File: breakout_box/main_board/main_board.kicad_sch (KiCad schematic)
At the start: 35 parts, among them CN1 19PIN_LEMO, Q1 DMP3099L, Q2 MJD122

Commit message: Update schematics
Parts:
- C1, C2, C3, C4: footprint main_board:140CLH-1010 -> Capacitor_SMD:CP_Elec_10x10; symbol main_board-eagle-import:CPOL-EU140CLH-1010 -> Device:C_Polarized
- C5, C6: symbol main_board-eagle-import:C-EUC0603 -> Device:C
- H1, H2: symbol main_board-eagle-import:MA20-1 -> Connector_Generic:Conn_01x20
- H17, H3, H4, H7, H8: symbol main_board-eagle-import:MA08-1 -> Connector_Generic:Conn_01x08
- JP1, JP10, JP11, JP12, JP13, JP2, JP3, JP4, JP5, JP6, JP7, JP8, JP9: symbol main_board-eagle-import:PINHD-1X03_2.00 -> Connector_Generic:Conn_01x03
- R1, R2, R3: symbol main_board-eagle-import:R-EU_R0603 -> Device:R
- R4: symbol main_board-eagle-import:R-EU_R0402 -> Device:R
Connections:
- net GND: now also C1.2, C2.2, C3.2, C4.2; no longer C1.-, C2.-, C3.-, C4.-
- net V_AUX: now also C1.1; no longer C1.+
- net V_OUT: now also C4.1; no longer C4.+
- net at Q2.1 (B), R2.1, R3.2: now also C3.1; no longer C3.+
- net at R1.1, R2.2: now also C2.1; no longer C2.+
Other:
- note added: "19P LEMO Connector"
- note removed: "AGND"
- note removed: "CH1"
- note removed: "CH10"
- note removed: "CH10_A"
- note removed: "CH10_CV"
- note removed: "CH11"
- note removed: "CH11_A"
- note removed: "CH12"
- note removed: "CH12_A"
- note removed: "CH13"
- note removed: "CH13_A"
- note removed: "CH14"
- note removed: "CH14_A"
- note removed: "CH15"
- note removed: "CH15_A"
- note removed: "CH2"
- note removed: "CH3"
- note removed: "CH4"
- note removed: "CH5"
- note removed: "CH6"
- note removed: "CH7"
- note removed: "CH8"
- note removed: "CH9"
- note removed: "CH9_A"
- note removed: "DGND"
- note removed: "From 19P LEMO Connector"
- note removed: "V_AUX"
- note removed: "V_OUT"
- moved on the sheet: CN1, LED1, Q1, Q2

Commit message: Bump version to 2.6
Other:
- note removed: "v2.5"
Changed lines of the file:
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@@
   (title_block
     (title "Nexus Main Board")
-    (date "2022-08-29")
-    (rev "2.51")
+    (date "2023-03-05")
+    (rev "2.6")
     (company "Document Number: 2022011")
   )
@@
     (effects (font (size 2.54 2.159)) (justify right bottom))
   )
-  (text "v2.5" (at 408.94 276.86 180)
-    (effects (font (size 2.54 2.54)) (justify left bottom))
-  )
   (text "GND" (at 128.905 201.295 180)

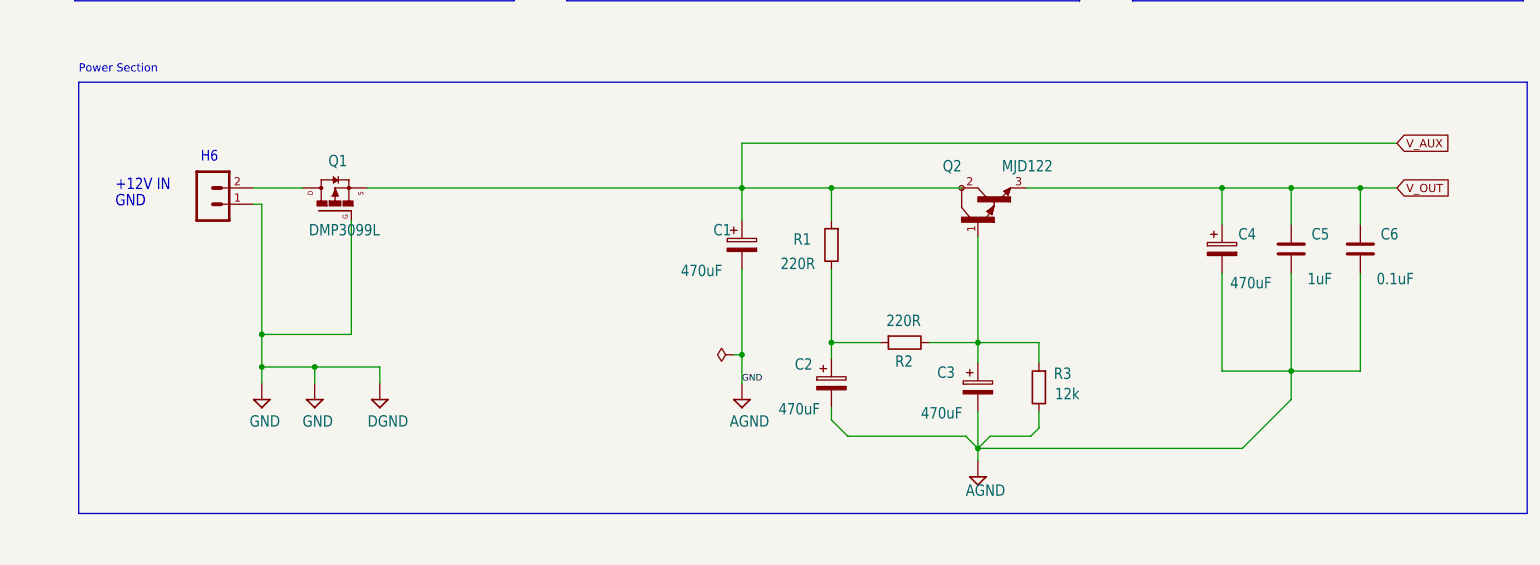
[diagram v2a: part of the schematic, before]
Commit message: Upgrade to v2.6 - Added short circuit protection - Added soft power switch - Various schematics and PCB layout updates
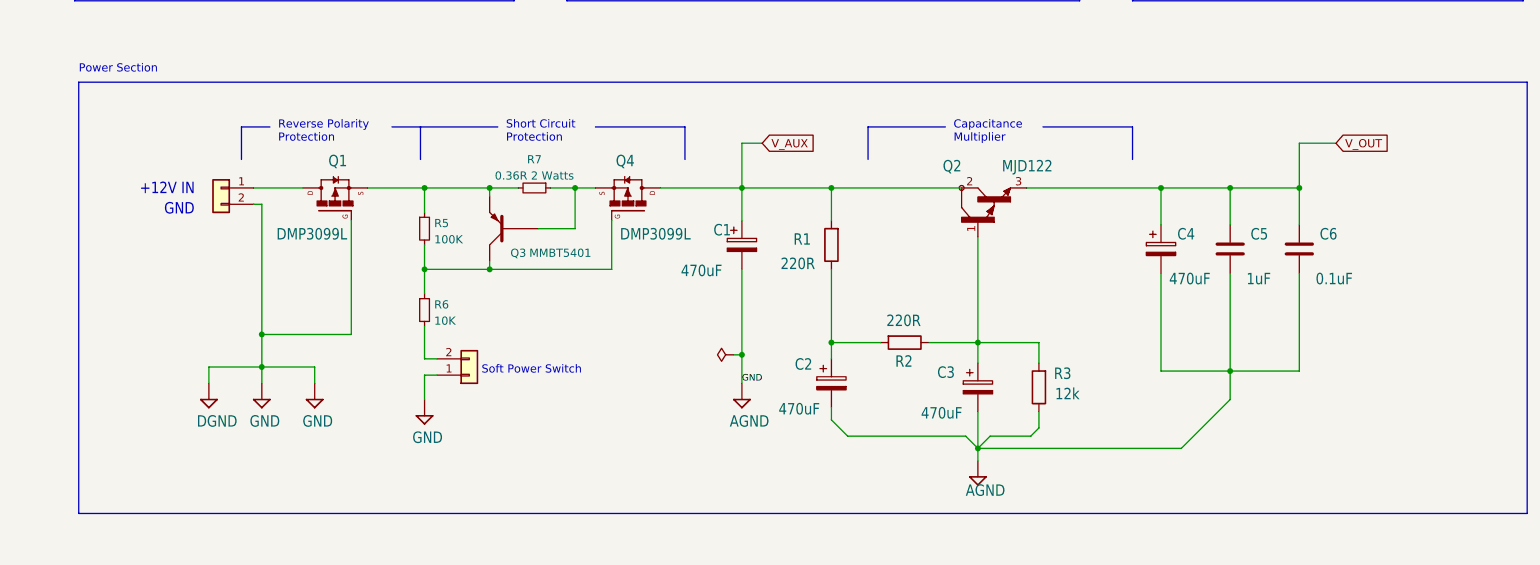
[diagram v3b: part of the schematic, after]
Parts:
- added H5: MA02-1, Connector_PinHeader_2.54mm:PinHeader_1x02_P2.54mm_Vertical, symbol Connector_Generic:Conn_01x02
- added Q3: MMBT5401, Package_TO_SOT_SMD:SOT-23, symbol Device:Q_PNP_BEC
- added Q4: DMP3099L, Package_TO_SOT_SMD:SOT-23, symbol main_board-eagle-import:P_MOSFET
- added R5: 100K, Resistor_SMD:R_0402_1005Metric, symbol Device:R_Small
- added R6: 10K, Resistor_SMD:R_0402_1005Metric, symbol Device:R_Small
- added R7: 0.36R 2 Watts, Resistor_SMD:R_2512_6332Metric, symbol Device:R_Small
- H6: footprint main_board:MA02-1 -> Connector_PinHeader_2.54mm:PinHeader_1x02_P2.54mm_Horizontal; symbol main_board-eagle-import:MA02-1 -> Connector_Generic:Conn_01x02
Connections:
- net GND: now also H6.2 (Pin_2), H5.1 (Pin_1); no longer H6.1
- net V_AUX: now also Q4.3 (D); no longer Q1.2 (S)
- net at Q1.3 (D): now also H6.1 (Pin_1); no longer H6.2
- new net: Q3.1 (B), Q4.2 (S), R7.1
- new net: Q1.2 (S), Q3.2 (E), R5.1, R7.2
- new net: Q3.3 (C), Q4.1 (G), R5.2, R6.1
- new net: H5.2 (Pin_2), R6.2
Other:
- note added: "Capacitance Multiplier"
- note added: "Reverse Polarity Protection"
- note added: "Short Circuit Protection"
- note added: "Soft Power Switch"
- note removed: "H6"
- moved on the sheet: C4, C5, C6

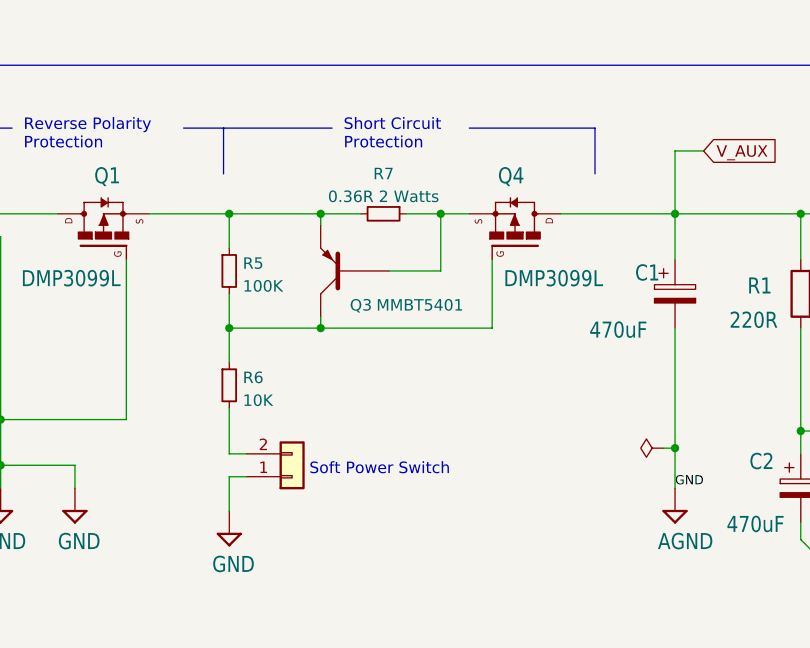
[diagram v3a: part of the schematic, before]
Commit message: two 1W resistors instead of one 2W resistor
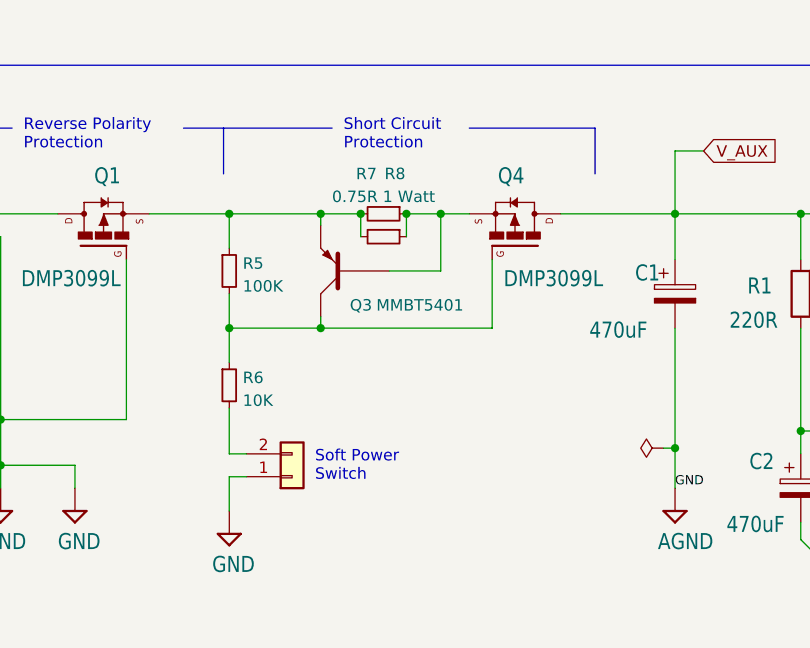
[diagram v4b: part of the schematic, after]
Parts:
- added R8: 0.75R 1 Watt, Resistor_SMD:R_2512_6332Metric, symbol Device:R_Small
- R7: value 0.36R 2 Watts -> 0.75R 1 Watt; LCSC C1712932 -> C621284
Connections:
- net at Q3.1 (B), Q4.2 (S), R7.1: now also R8.1
- net at Q1.2 (S), Q3.2 (E), R5.1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: now also R8.2
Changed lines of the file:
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@@
   (junction (at 292.1 198.12) (diameter 0) (color 0 0 0 0)
   )
+  (junction (at 196.85 198.12) (diameter 0) (color 0 0 0 0)
+  )
   (junction (at 311.15 129.54) (diameter 0) (color 0 0 0 0)
   )
@@
   (junction (at 223.52 80.645) (diameter 0) (color 0 0 0 0)
   )
+  (junction (at 191.77 198.12) (diameter 0) (color 0 0 0 0)
+  )
   (junction (at 223.52 70.485) (diameter 0) (color 0 0 0 0)
   )
@@
     (stroke (width 0) (type default) (color 0 0 0 0))
   )
+  (wire (pts (xy 196.85 198.12) (xy 196.85 200.66))
+    (stroke (width 0) (type default) (color 0 0 0 0))
+  )
   (wire (pts (xy 92.075 90.17) (xy 92.075 93.345))
     (stroke (width 0) (type default) (color 0 0 0 0))
@@
   )
   (wire (pts (xy 175.895 65.405) (xy 179.07 65.405))
+    (stroke (width 0) (type default) (color 0 0 0 0))
+  )
+  (wire (pts (xy 191.77 198.12) (xy 191.77 200.66))
     (stroke (width 0) (type default) (color 0 0 0 0))
   )
@@
     (effects (font (size 1.778 1.5113)) (justify left bottom))
   )
-  (text "Soft Power Switch" (at 186.055 227.33 0)
+  (text "Soft Power \nSwitch" (at 186.69 227.965 0)
     (effects (font (size 1.27 1.27)) (justify left bottom))
   )
@@
   )
   (symbol (lib_id "Device:R_Small") (at 194.31 198.12 270) (unit 1)
-    (in_bom yes) (on_board yes) (fields_autoplaced)
-    (property "Reference" "R7" (id 0) (at 194.31 193.6836 90))
-    (property "Value" "0.36R 2 Watts" (id 1) (at 194.31 196.2205 90))
+    (in_bom yes) (on_board yes)
+    (property "Reference" "R7" (id 0) (at 192.405 193.6836 90))
+    (property "Value" "0.75R 1 Watt" (id 1) (at 194.31 196.2205 90))
     (property "Footprint" "Resistor_SMD:R_2512_6332Metric" (id 2) (at 194.31 198.12 0)
       (effects (font (size 1.27 1.27)) hide)
@@
       (effects (font (size 1.27 1.27)) hide)
     )
-    (property "LCSC" "C1712932" (id 4) (at 194.31 198.12 0)
+    (property "LCSC" "C621284" (id 4) (at 194.31 198.12 0)
       (effects (font (size 1.27 1.27)) hide)
     )
@@
     (pin "9")
   )
+  (symbol (lib_id "Device:R_Small") (at 194.31 200.66 270) (unit 1)
+    (in_bom yes) (on_board yes)
+    (property "Reference" "R8" (id 0) (at 195.58 193.675 90))
+    (property "Value" "0.75R 1 Watt" (id 1) (at 194.31 198.7605 90)
+      (effects (font (size 1.27 1.27)) hide)
+    )
+    (property "Footprint" "Resistor_SMD:R_2512_6332Metric" (id 2) (at 194.31 200.66 0)
+      (effects (font (size 1.27 1.27)) hide)
+    )
+    (property "Datasheet" "~" (id 3) (at 194.31 200.66 0)
+      (effects (font (size 1.27 1.27)) hide)
+    )
+    (property "LCSC" "C621284" (id 4) (at 194.31 200.66 0)
+      (effects (font (size 1.27 1.27)) hide)
+    )
+    (pin "1")
+    (pin "2")
+  )
   (symbol (lib_id "main_board-eagle-import:TIP122") (at 263.525 200.66 90) (unit 1)
     (in_bom yes) (on_board yes)
@@
     )
     (path "/8d602f51-ddcc-462d-b7b1-e1315390fda3"
-      (reference "R7") (unit 1) (value "0.36R 2 Watts") (footprint "Resistor_SMD:R_2512_6332Metric")
-    )
-  )
+      (reference "R7") (unit 1) (value "0.75R 1 Watt") (footprint "Resistor_SMD:R_2512_6332Metric")
+    )
+    (path "/f7adad24-fc33-44f9-a5b5-dccfe69ddd60"
+      (reference "R8") (unit 1) (value "0.75R 1 Watt") (footprint "Resistor_SMD:R_2512_6332Metric")
+    )
+  )

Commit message: some tweaks
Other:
- moved on the sheet: LED1, R4
